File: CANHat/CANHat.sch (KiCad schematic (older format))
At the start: 1 part, among them J0 RPi_GPIO

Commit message: Small typo error fixed
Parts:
- added C1: 10 uf, ~, symbol CP1
- added C2, C4: 22 pf, ~, symbol C
- added C3, C6: .1 uf, ~, symbol C
- added C5: 15 uf, ~, symbol CP1
- added J1: SPI Select, SIL-3, symbol CONN_3
- added J2, J3: RJ45, ~, symbol RJ45
- added R1: 10K Ohms, ~, symbol R
- added U1: MCP2515, DIL-18_300, symbol MCP2515
- added U2: MCP2551, DIL-8_300, symbol MCP2551
- added X1: 8 MHz, ~, symbol CRYSTAL
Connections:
- net VDD: now reaches J0.1 (3.3V)
- net VDD: now also C1.1, C3.1, R1.1, U1.18 (Vcc)
- net at J0.19 (BCM10_MOSI): now also U1.14 (SI)
- net at J0.21 (BCM9_MISO): now also U1.15 (SO)
- net at J0.23 (BCM11_SCLK): now also U1.13 (SCK)
- net at J0.24 (BCM8_CE0): now also J1.1 (P1)
- net at J0.26 (BCM7_CE1): now also J1.3 (P3)
- net at J0.32 (BCM12): now also U1.12 (INT)
- net VCC: now reaches J0.4 (5V)
- net VCC: now also C5.1, C6.1, U2.3 (Vcc)
- net GND: now reaches J0.6 (GND)
- net GND: now also C1.2, C2.2, C3.2, C4.2, C5.2, C6.2, J2.9 (SHIELD), J3.9 (SHIELD), U1.9 (GND), U2.2 (GND), U2.8 (Rs)
- new net: U1.1 (TXCAN), U2.1 (TXD)
- new net: J1.2 (PM), U1.16 (CS)
- new net: R1.2, U1.17 (RST)
- new net: U1.2 (RXCAN), U2.4 (RXD)
- new net: C4.1, U1.7 (OSC2), X1.2
- new net: C2.1, U1.8 (OSC1), X1.1
- new net: J2.2, J3.2, U2.6 (CANL)
- new net: J2.1, J3.1, U2.7 (CANH)
- new net: J2.3, J3.3
- new net: J2.4, J3.4
- new net: J2.5, J3.5
- new net: J2.6, J3.6
- new net: J2.7, J3.7
- new net: J2.8, J3.8
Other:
- moved on the sheet: J0

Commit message: Completed CAN Hat
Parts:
- C1: footprint ~ -> C1V5; Mouser part Number (none) -> 667-ECA-1HM100I
- C2, C4: footprint ~ -> C2; Mouser part number (none) -> 594-K220J10C0GF5UH5
- C3: footprint ~ -> C1; Mouser Part Number (none) -> 21RZ310-RC
- C5: footprint ~ -> C1V7; Mouser part number (none) -> 667-EEA-GA1H150
- C6: footprint ~ -> C1; Mouser Part number (none) -> 21RZ310-RC
- J0: Adafruit part number (none) -> 2223; Mouser part number (none) -> 517-929975-01-20
- J1: footprint SIL-3 -> PIN_ARRAY_3X1; Mouser part number (none) -> 538-22-28-8034
- J2, J3: footprint ~ -> RJ45-8N-S; Mouser part number (none) -> 592-RJ45-8N-S
- R1: footprint ~ -> R1; Mouser part number (none) -> 603-CFR-25JR-5210K
- U1: footprint DIL-18_300 -> DIP-18_300; Mouser part number (none) -> 579-MCP2515-I/P
- U2: footprint DIL-8_300 -> DIP-8_300; Mouser part number (none) -> 579-MCP2551-I/P
- X1: footprint ~ -> HC-49V; Mouser part number (none) -> 449-LFXTAL029488BULK
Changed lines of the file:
@@
 F 2 "RPi_Hat:Pin_Header_Straight_2x20" H 1200 1100 60  0001 C CNN
 F 3 "" H 1200 1100 60  0000 C CNN
+F 4 "517-929975-01-20" H 1200 1100 60  0001 C CNN "Mouser part number"
+F 5 "2223" H 1200 1100 60  0001 C CNN "Adafruit part number"
 	1    1200 1100
 	1    0    0    -1
@@
 F 0 "U1" H 2800 4650 60  0000 C CNN
 F 1 "MCP2515" H 2800 5050 60  0000 C CNN
-F 2 "DIL-18_300" H 2700 4850 60  0001 C CNN
+F 2 "DIP-18_300" H 2700 4850 60  0001 C CNN
 F 3 "" H 2800 4950 60  0000 C CNN
+F 4 "579-MCP2515-I/P" H 2800 4950 60  0001 C CNN "Mouser part number"
 	1    2800 4950
 	1    0    0    -1
@@
 F 0 "U2" H 5950 5100 60  0000 C CNN
 F 1 "MCP2551" H 5950 5200 60  0000 C CNN
-F 2 "DIL-8_300" H 5950 5000 60  0001 C CNN
+F 2 "DIP-8_300" H 5950 5000 60  0001 C CNN
 F 3 "" H 5950 5100 60  0000 C CNN
+F 4 "579-MCP2551-I/P" H 5950 5100 60  0001 C CNN "Mouser part number"
 	1    5950 5100
 	1    0    0    -1
@@
 F 0 "J2" H 10050 4100 60  0000 C CNN
 F 1 "RJ45" H 9700 4100 60  0000 C CNN
-F 2 "~" H 9850 3600 60  0000 C CNN
+F 2 "RJ45-8N-S" H 9850 3600 60  0001 C CNN
 F 3 "~" H 9850 3600 60  0000 C CNN
+F 4 "592-RJ45-8N-S" H 9850 3600 60  0001 C CNN "Mouser part number"
 	1    9850 3600
 	0    1    1    0
@@
 F 0 "J3" H 10100 6100 60  0000 C CNN
 F 1 "RJ45" H 9750 6100 60  0000 C CNN
-F 2 "~" H 9900 5600 60  0000 C CNN
+F 2 "RJ45-8N-S" H 9900 5600 60  0001 C CNN
 F 3 "~" H 9900 5600 60  0000 C CNN
+F 4 "592-RJ45-8N-S" H 9900 5600 60  0001 C CNN "Mouser part number"
 	1    9900 5600
 	0    1    1    0
@@
 F 0 "R1" V 2030 4250 40  0000 C CNN
 F 1 "10K Ohms" V 1957 4251 40  0000 C CNN
-F 2 "~" V 1880 4250 30  0000 C CNN
+F 2 "R1" V 1880 4250 30  0001 C CNN
 F 3 "~" H 1950 4250 30  0000 C CNN
+F 4 "603-CFR-25JR-5210K" V 1950 4250 60  0001 C CNN "Mouser part number"
 	1    1950 4250
 	1    0    0    -1
@@
 F 0 "J1" V 850 4900 50  0000 C CNN
 F 1 "SPI Select" V 950 4900 40  0000 C CNN
-F 2 "SIL-3" H 900 4900 60  0001 C CNN
+F 2 "PIN_ARRAY_3X1" H 900 4900 60  0001 C CNN
 F 3 "~" H 900 4900 60  0000 C CNN
+F 4 "538-22-28-8034" V 900 4900 60  0001 C CNN "Mouser part number"
 	1    900  4900
 	-1   0    0    1
@@
 F 0 "C3" H 1500 4300 40  0000 L CNN
 F 1 ".1 uf" H 1506 4115 40  0000 L CNN
-F 2 "~" H 1538 4050 30  0000 C CNN
+F 2 "C1" H 1538 4050 30  0001 C CNN
 F 3 "~" H 1500 4200 60  0000 C CNN
+F 4 "21RZ310-RC" H 1500 4200 60  0001 C CNN "Mouser Part Number"
 	1    1500 4200
 	1    0    0    -1
@@
 F 0 "C1" H 1150 4300 50  0000 L CNN
 F 1 "10 uf" H 1150 4100 50  0000 L CNN
-F 2 "~" H 1100 4200 60  0000 C CNN
+F 2 "C1V5" H 1100 4200 60  0001 C CNN
 F 3 "~" H 1100 4200 60  0000 C CNN
+F 4 "667-ECA-1HM100I" H 1100 4200 60  0001 C CNN "Mouser part Number"
 	1    1100 4200
 	1    0    0    -1
@@
 F 0 "C5" H 6600 4500 50  0000 L CNN
 F 1 "15 uf" H 6600 4300 50  0000 L CNN
-F 2 "~" H 6550 4400 60  0000 C CNN
-F 3 "~" H 6550 4400 60  0000 C CNN
+F 2 "C1V7" H 6550 4400 60  0001 C CNN
+F 3 "~" H 6550 4400 60  0001 C CNN
+F 4 "667-EEA-GA1H150" H 6550 4400 60  0001 C CNN "Mouser part number"
 	1    6550 4400
 	1    0    0    -1
@@
 F 0 "C6" H 7000 4500 40  0000 L CNN
 F 1 ".1 uf" H 7006 4315 40  0000 L CNN
-F 2 "~" H 7038 4250 30  0000 C CNN
+F 2 "C1" H 7038 4250 30  0001 C CNN
 F 3 "~" H 7000 4400 60  0000 C CNN
+F 4 "21RZ310-RC" H 7000 4400 60  0001 C CNN "Mouser Part number"
 	1    7000 4400
 	1    0    0    -1
@@
 F 0 "X1" H 1600 6100 60  0000 C CNN
 F 1 "8 MHz" H 1600 5800 60  0000 C CNN
-F 2 "~" H 1600 5950 60  0000 C CNN
+F 2 "HC-49V" H 1600 5950 60  0001 C CNN
 F 3 "~" H 1600 5950 60  0000 C CNN
+F 4 "449-LFXTAL029488BULK" H 1600 5950 60  0001 C CNN "Mouser part number"
 	1    1600 5950
 	1    0    0    -1
@@
 F 0 "C2" H 1300 6350 40  0000 L CNN
 F 1 "22 pf" H 1306 6165 40  0000 L CNN
-F 2 "~" H 1338 6100 30  0000 C CNN
+F 2 "C2" H 1338 6100 30  0001 C CNN
 F 3 "~" H 1300 6250 60  0000 C CNN
+F 4 "594-K220J10C0GF5UH5" H 1300 6250 60  0001 C CNN "Mouser part number"
 	1    1300 6250
 	1    0    0    -1
@@
 F 0 "C4" H 1900 6350 40  0000 L CNN
 F 1 "22 pf" H 1906 6165 40  0000 L CNN
-F 2 "~" H 1938 6100 30  0000 C CNN
+F 2 "C2" H 1938 6100 30  0001 C CNN
 F 3 "~" H 1900 6250 60  0000 C CNN
+F 4 "594-K220J10C0GF5UH5" H 1900 6250 60  0001 C CNN "Mouser part number"
 	1    1900 6250
 	1    0    0    -1

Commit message: Updated part  number for the crystal (correct load cap.).
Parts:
- X1: Mouser part number 449-LFXTAL029488BULK -> 449-LFXTAL031818BULK
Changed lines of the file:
@@
 F 2 "HC-49V" H 1600 5950 60  0001 C CNN
 F 3 "~" H 1600 5950 60  0000 C CNN
-F 4 "449-LFXTAL029488BULK" H 1600 5950 60  0001 C CNN "Mouser part number"
+F 4 "449-LFXTAL031818BULK " H 1600 5950 60  0001 C CNN "Mouser part number"
 	1    1600 5950
 	1    0    0    -1

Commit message: Update sheet settings, change header to stacking.
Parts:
- J0: Mouser part number 517-929975-01-20 -> 855-M20-6102045
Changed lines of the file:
@@
 EELAYER 27 0
 EELAYER END
-$Descr A4 11693 8268
+$Descr USLetter 11000 8500
 encoding utf-8
 Sheet 1 1
-Title ""
-Date "20 apr 2017"
+Title "CAN Bus (MCP2515) Hat"
+Date "25 apr 2017"
 Rev ""
-Comp ""
+Comp "Deepwoods Software"
 Comment1 ""
 Comment2 ""
@@
 F 2 "RPi_Hat:Pin_Header_Straight_2x20" H 1200 1100 60  0001 C CNN
 F 3 "" H 1200 1100 60  0000 C CNN
-F 4 "517-929975-01-20" H 1200 1100 60  0001 C CNN "Mouser part number"
+F 4 "855-M20-6102045" H 1200 1100 60  0001 C CNN "Mouser part number"
 F 5 "2223" H 1200 1100 60  0001 C CNN "Adafruit part number"
 	1    1200 1100

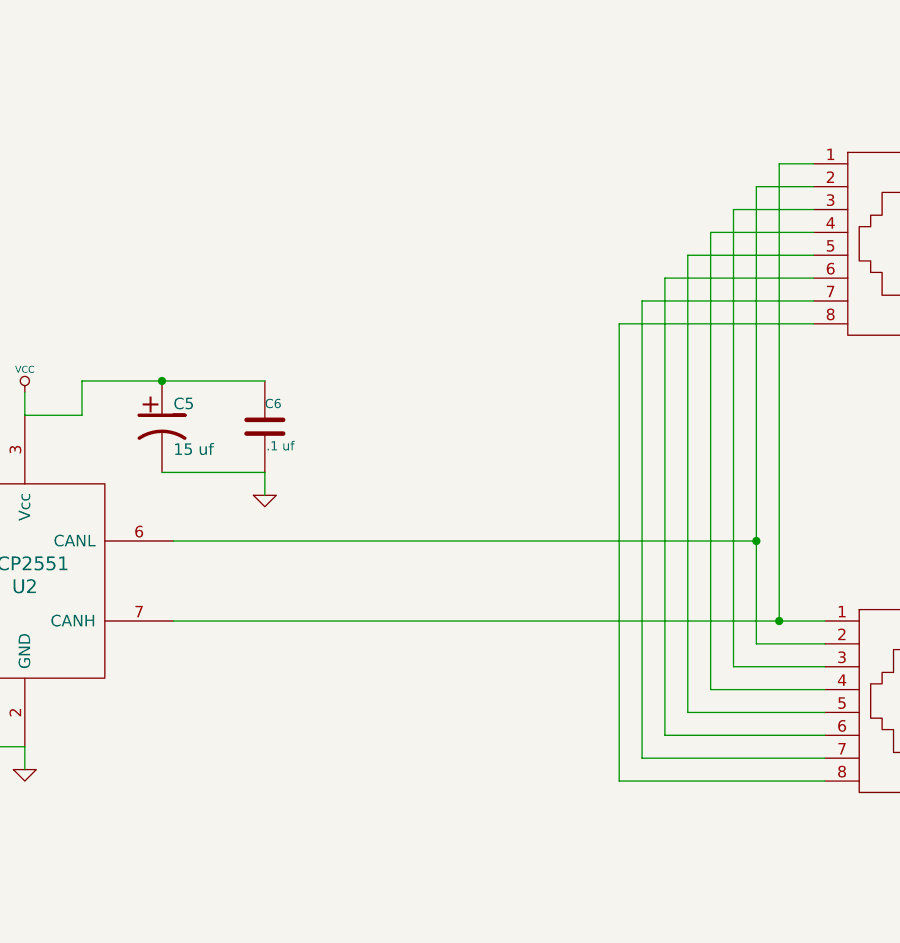
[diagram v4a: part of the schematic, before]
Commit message: Add power injection and CAN shield and CAN ground connections to the CAN connectors.
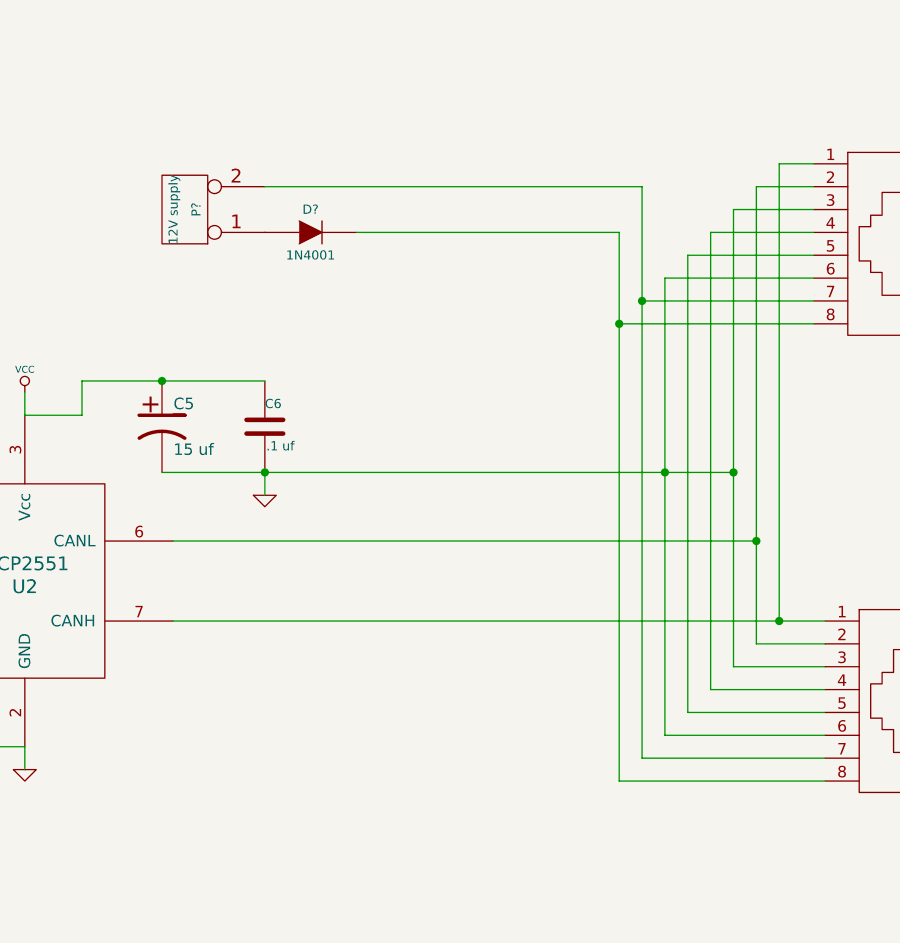
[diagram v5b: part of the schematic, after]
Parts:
- added D?: 1N4001, ~, symbol DIODE
- added P?: 12V supply, ~, symbol CONN_2
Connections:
- net GND: now also J2.3, J2.6, J3.3, J3.6
- net at J2.7, J3.7: now also P?.2 (PM)
- net at J2.8, J3.8: now also D?.2 (K)
- new net: D?.1 (A), P?.1 (P1)
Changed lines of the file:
@@
 Sheet 1 1
 Title "CAN Bus (MCP2515) Hat"
-Date "25 apr 2017"
+Date "28 apr 2017"
 Rev ""
 Comp "Deepwoods Software"
@@
 Connection ~ 6550 4200
 Wire Wire Line
-	6550 4600 7000 4600
+	6550 4600 9050 4600
 $Comp
 L GND #PWR09
@@
 	9400 3850 8650 3850
 Wire Wire Line
-	8650 3850 8650 5850
+	8650 3350 8650 5850
 Wire Wire Line
 	8650 5850 9450 5850
@@
 	9400 3950 8550 3950
 Wire Wire Line
-	8550 3950 8550 5950
+	8550 3550 8550 5950
 Wire Wire Line
 	8550 5950 9450 5950
@@
 Wire Wire Line
 	10200 4150 10200 4350
+$Comp
+L CONN_2 P?
+U 1 1 590378B2
+P 6650 3450
+F 0 "P?" V 6600 3450 40  0000 C CNN
+F 1 "12V supply" V 6700 3450 40  0000 C CNN
+F 2 "~" H 6650 3450 60  0000 C CNN
+F 3 "~" H 6650 3450 60  0000 C CNN
+	1    6650 3450
+	-1   0    0    1
+$EndComp
+$Comp
+L DIODE D?
+U 1 1 590378E2
+P 7200 3550
+F 0 "D?" H 7200 3650 40  0000 C CNN
+F 1 "1N4001" H 7200 3450 40  0000 C CNN
+F 2 "~" H 7200 3550 60  0000 C CNN
+F 3 "~" H 7200 3550 60  0000 C CNN
+	1    7200 3550
+	1    0    0    -1
+$EndComp
+Wire Wire Line
+	7400 3550 8550 3550
+Connection ~ 8550 3950
+Wire Wire Line
+	7000 3350 8650 3350
+Connection ~ 8650 3850
+Connection ~ 8750 4600
+Connection ~ 9050 4600
+Connection ~ 7000 4600
 $EndSCHEMATC

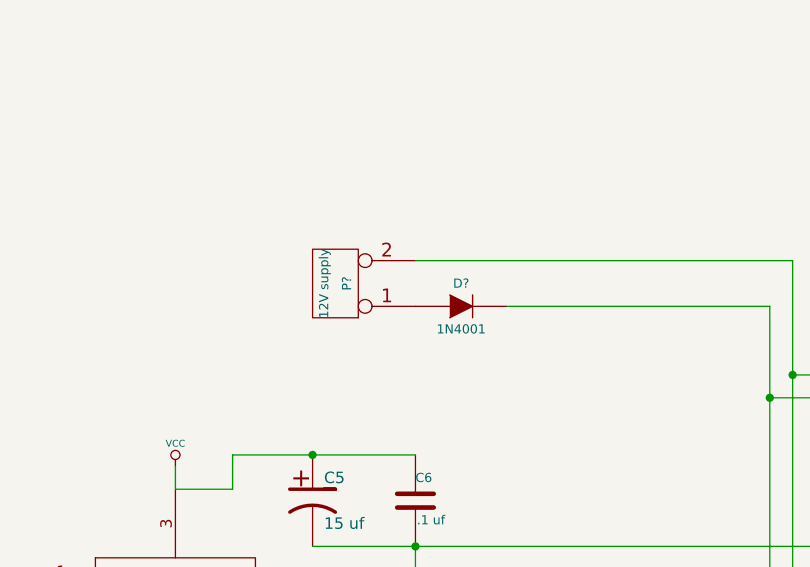
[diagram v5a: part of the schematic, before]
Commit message: Add footprints for power injection and update PCB to include power injection and CAN ground and shield.
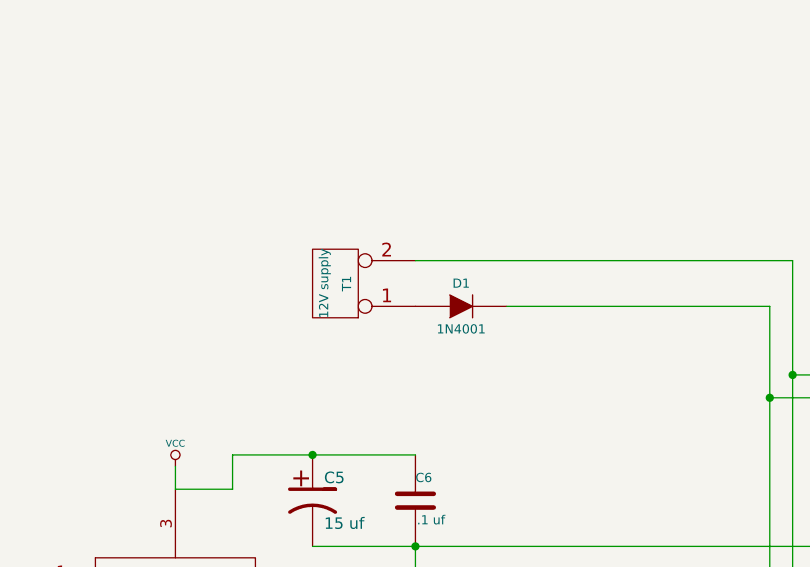
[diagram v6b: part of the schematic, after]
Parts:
- D1: renamed from D?; footprint ~ -> D3; Mouser Part Number (none) -> 833-1N4001-TP
- T1: renamed from P?; footprint ~ -> bornier2; Mouser Part Number (none) -> 571-1776118-2
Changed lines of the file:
@@
 	10200 4150 10200 4350
 $Comp
-L CONN_2 P?
+L CONN_2 T1
 U 1 1 590378B2
 P 6650 3450
-F 0 "P?" V 6600 3450 40  0000 C CNN
+F 0 "T1" V 6600 3450 40  0000 C CNN
 F 1 "12V supply" V 6700 3450 40  0000 C CNN
-F 2 "~" H 6650 3450 60  0000 C CNN
+F 2 "bornier2" H 6650 3450 60  0001 C CNN
 F 3 "~" H 6650 3450 60  0000 C CNN
+F 4 "571-1776118-2" V 6650 3450 60  0001 C CNN "Mouser Part Number"
 	1    6650 3450
 	-1   0    0    1
 $EndComp
 $Comp
-L DIODE D?
+L DIODE D1
 U 1 1 590378E2
 P 7200 3550
-F 0 "D?" H 7200 3650 40  0000 C CNN
+F 0 "D1" H 7200 3650 40  0000 C CNN
 F 1 "1N4001" H 7200 3450 40  0000 C CNN
-F 2 "~" H 7200 3550 60  0000 C CNN
+F 2 "D3" H 7200 3550 60  0001 C CNN
 F 3 "~" H 7200 3550 60  0000 C CNN
+F 4 "833-1N4001-TP" H 7200 3550 60  0001 C CNN "Mouser Part Number"
 	1    7200 3550
 	1    0    0    -1

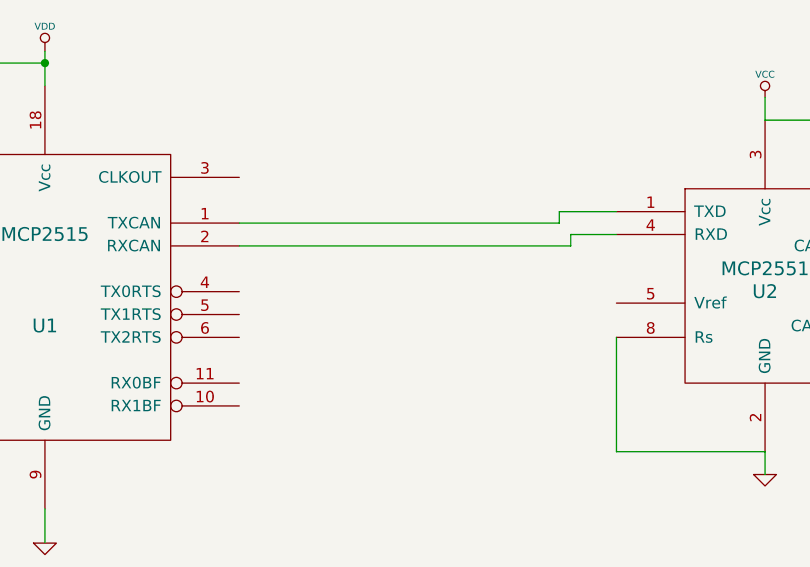
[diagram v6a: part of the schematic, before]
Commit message: Add level shifting tranceiver => controller (RXD => RXCAN).
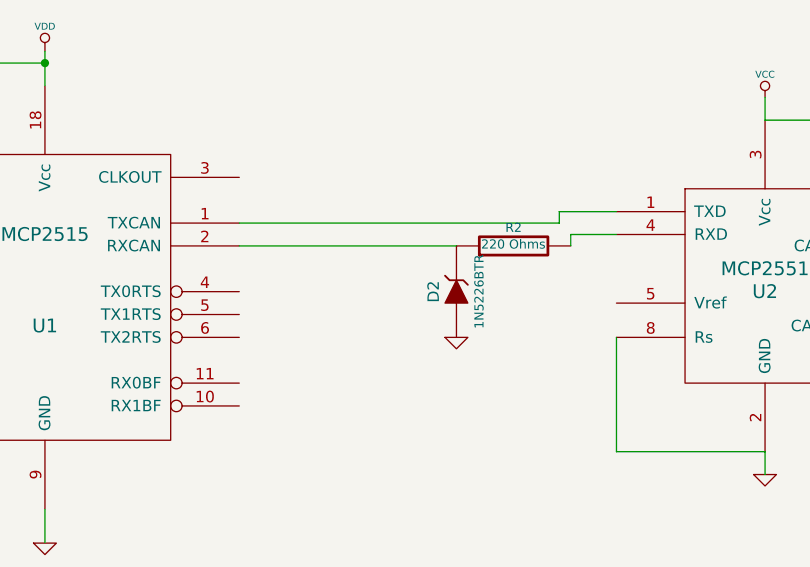
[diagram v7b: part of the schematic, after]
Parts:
- added D2: 1N5226BTR, ~, symbol ZENER
- added R2: 220 Ohms, ~, symbol R
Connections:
- net GND: now also D2.1 (A)
- net at U1.2 (RXCAN): now also D2.2 (K), R2.1; no longer U2.4 (RXD)
- new net: R2.2, U2.4 (RXD)
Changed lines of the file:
@@
 Sheet 1 1
 Title "CAN Bus (MCP2515) Hat"
-Date "28 apr 2017"
+Date "5 jul 2017"
 Rev ""
 Comp "Deepwoods Software"
@@
 	5050 4750 5300 4750
 Wire Wire Line
-	3650 4900 5100 4900
-Wire Wire Line
 	5100 4900 5100 4850
 Wire Wire Line
@@
 Connection ~ 9050 4600
 Connection ~ 7000 4600
+$Comp
+L R R2
+U 1 1 595D3071
+P 4850 4900
+F 0 "R2" V 4930 4900 40  0000 C CNN
+F 1 "220 Ohms" V 4857 4901 40  0000 C CNN
+F 2 "~" V 4780 4900 30  0000 C CNN
+F 3 "~" H 4850 4900 30  0000 C CNN
+	1    4850 4900
+	0    -1   -1   0
+$EndComp
+$Comp
+L ZENER D2
+U 1 1 595D308E
+P 4600 5100
+F 0 "D2" H 4600 5200 50  0000 C CNN
+F 1 "1N5226BTR" H 4600 5000 40  0000 C CNN
+F 2 "~" H 4600 5100 60  0000 C CNN
+F 3 "~" H 4600 5100 60  0000 C CNN
+	1    4600 5100
+	0    -1   -1   0
+$EndComp
+Wire Wire Line
+	4600 4900 3650 4900
+$Comp
+L GND #PWR014
+U 1 1 595D310B
+P 4600 5300
+F 0 "#PWR014" H 4600 5300 30  0001 C CNN
+F 1 "GND" H 4600 5230 30  0001 C CNN
+F 2 "" H 4600 5300 60  0000 C CNN
+F 3 "" H 4600 5300 60  0000 C CNN
+	1    4600 5300
+	1    0    0    -1
+$EndComp
 $EndSCHEMATC

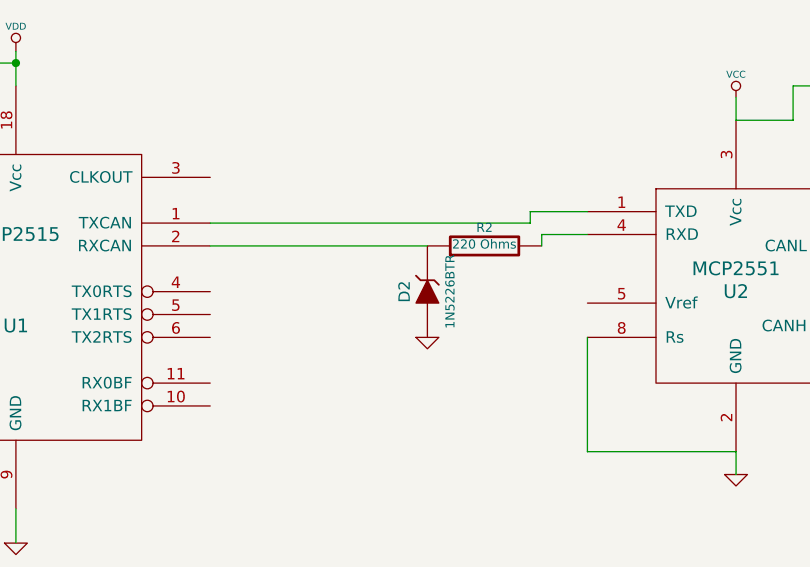
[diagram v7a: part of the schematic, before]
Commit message: Updates to CAN Hats (incomplete -- waiting on bandwidth)
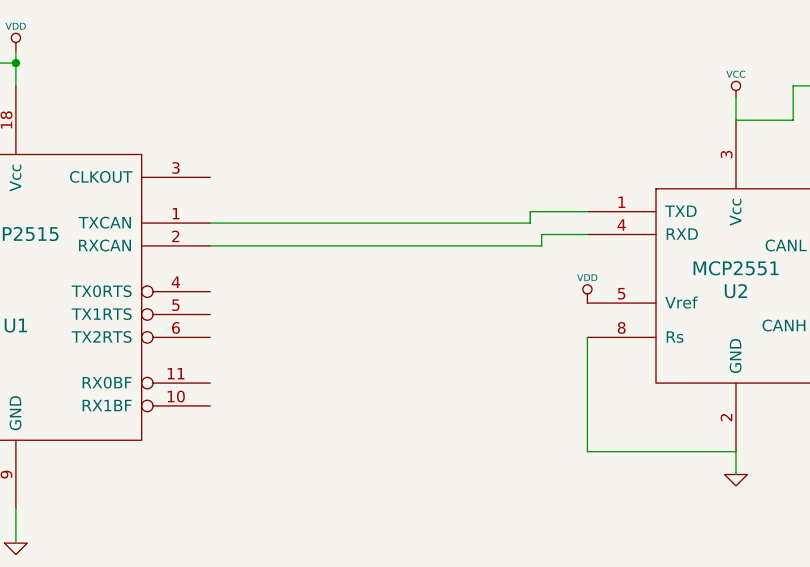
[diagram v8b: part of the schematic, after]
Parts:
- removed D2: 1N5226BTR, ~, symbol ZENER
- removed R2: 220 Ohms, ~, symbol R
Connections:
- net VDD: now also U2.5 (Vref)
- net at U1.2 (RXCAN): now also U2.4 (RXD)
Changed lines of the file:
@@
 Sheet 1 1
 Title "CAN Bus (MCP2515) Hat"
-Date "5 jul 2017"
+Date "21 feb 2018"
 Rev ""
 Comp "Deepwoods Software"
@@
 Connection ~ 9050 4600
 Connection ~ 7000 4600
-$Comp
-L R R2
-U 1 1 595D3071
-P 4850 4900
-F 0 "R2" V 4930 4900 40  0000 C CNN
-F 1 "220 Ohms" V 4857 4901 40  0000 C CNN
-F 2 "~" V 4780 4900 30  0000 C CNN
-F 3 "~" H 4850 4900 30  0000 C CNN
-	1    4850 4900
-	0    -1   -1   0
-$EndComp
-$Comp
-L ZENER D2
-U 1 1 595D308E
-P 4600 5100
-F 0 "D2" H 4600 5200 50  0000 C CNN
-F 1 "1N5226BTR" H 4600 5000 40  0000 C CNN
-F 2 "~" H 4600 5100 60  0000 C CNN
-F 3 "~" H 4600 5100 60  0000 C CNN
-	1    4600 5100
-	0    -1   -1   0
-$EndComp
-Wire Wire Line
-	4600 4900 3650 4900
-$Comp
-L GND #PWR014
-U 1 1 595D310B
-P 4600 5300
-F 0 "#PWR014" H 4600 5300 30  0001 C CNN
-F 1 "GND" H 4600 5230 30  0001 C CNN
-F 2 "" H 4600 5300 60  0000 C CNN
-F 3 "" H 4600 5300 60  0000 C CNN
-	1    4600 5300
-	1    0    0    -1
-$EndComp
+Wire Wire Line
+	3650 4900 5100 4900
+$Comp
+L VDD #PWR014
+U 1 1 5A8D8397
+P 5300 5150
+F 0 "#PWR014" H 5300 5250 30  0001 C CNN
+F 1 "VDD" H 5300 5260 30  0000 C CNN
+F 2 "" H 5300 5150 60  0000 C CNN
+F 3 "" H 5300 5150 60  0000 C CNN
+	1    5300 5150
+	1    0    0    -1
+$EndComp
